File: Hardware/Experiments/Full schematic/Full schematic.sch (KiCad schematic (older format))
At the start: 31 parts

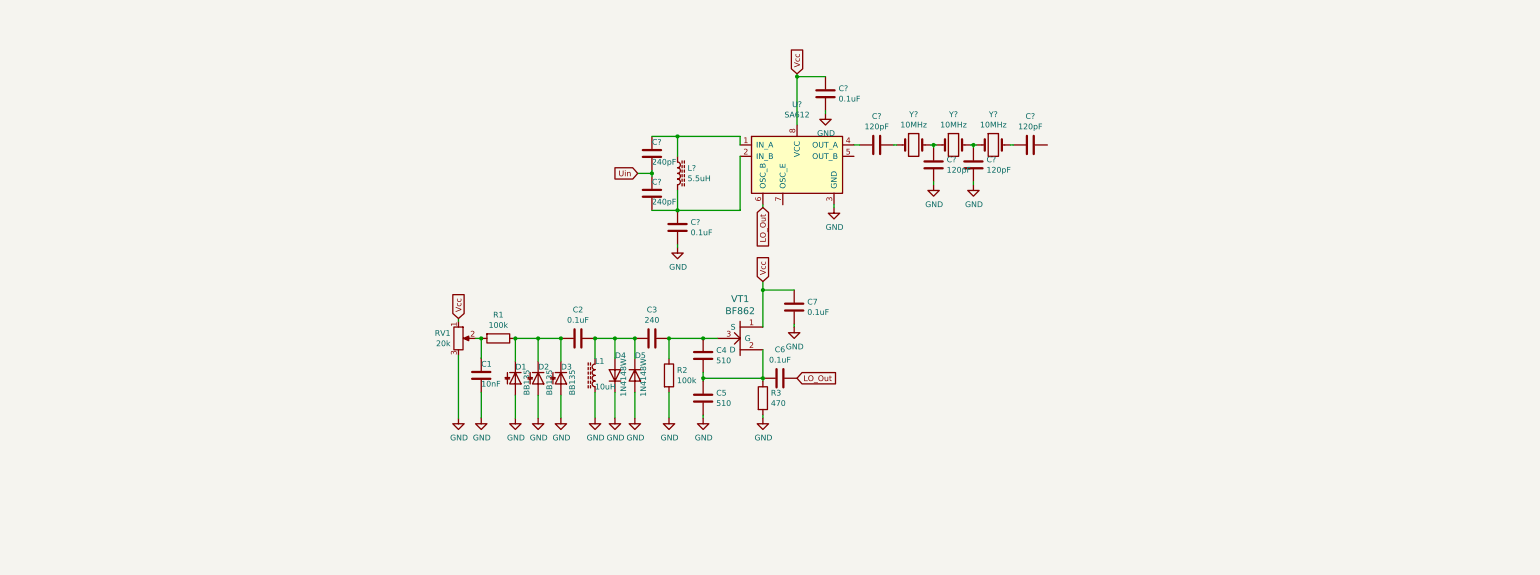
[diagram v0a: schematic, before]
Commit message: IF amplifier + second frequency convertor - tested IRL
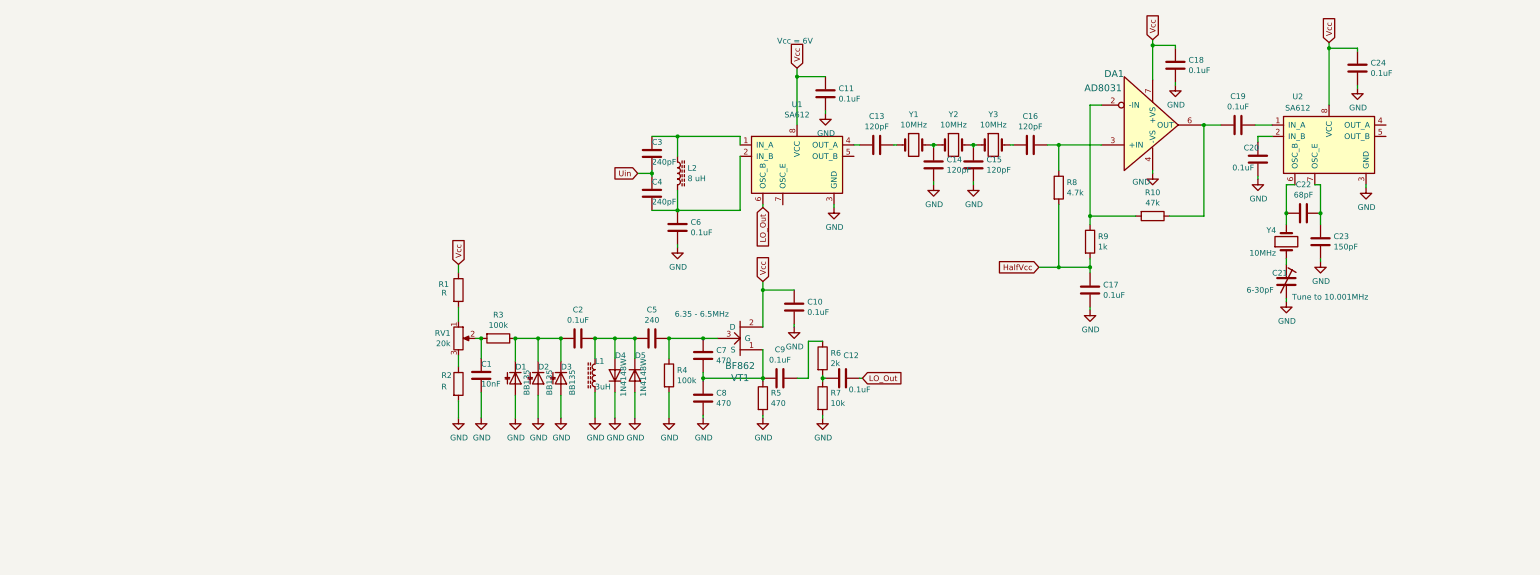
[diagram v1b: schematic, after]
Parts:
- added C12, C17, C18, C19, C20, C24: 0.1uF, symbol Device:C
- added C21: 6-30pF, symbol Device:CTRIM
- added C22: 68pF, symbol Device:C
- added C23: 150pF, symbol Device:C
- added DA1: AD8031, symbol Fossa_library:AD8031
- added R1, R2: R, symbol Device:R
- added R10: 47k, symbol Device:R
- added R6: 2k, symbol Device:R
- added R7: 10k, symbol Device:R
- added R8: 4.7k, symbol Device:R
- added R9: 1k, symbol Device:R
- added U2: SA612, symbol Fossa_library:SA612
- added Y4: 10MHz, symbol Device:Crystal
- C7: renamed from C4; value 510 -> 470
- C8: renamed from C5; value 510 -> 470
- L1: value 10uH -> 3uH
- L2: renamed from L?; value 5.5uH -> 8 uH
- gave numbers to parts that had none: 12
- renumbered C7 to C10, C3 to C5, C6 to C9, R1 to R3, R2 to R4, R3 to R5
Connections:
- net GND: now also C17.2, C18.2, C20.2, C21.2, C23.2, C24.2, DA1.4 (-VS), R2.2, R7.2, U2.3 (GND); no longer RV1.3
- net LO_Out: now also C12.1; no longer C9.1
- net Vcc: now also VT1.2 (D), C18.1, C24.1, DA1.7 (+VS), R1.1, U2.8 (VCC); no longer RV1.1, VT1.1 (S)
- net at C7.2, C8.1, C9.2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: now also VT1.1 (S); no longer VT1.2 (D)
- net at C16.2: now also DA1.3 (+IN), R8.1
- new net: R1.2, RV1.1
- new net: R2.1, RV1.3
- new net: C12.2, R6.2, R7.1
- new net: C9.1, R6.1
- new net: DA1.2 (-IN), R10.2, R9.1
- new net: C19.2, DA1.6 (OUT), R10.1
- new net: C19.1, U2.1 (IN_A)
- new net: C20.1, U2.2 (IN_B)
- new net: C22.2, U2.6 (OSC_B), Y4.2
- new net: C22.1, C23.1, U2.7 (OSC_E)
- new net: C21.1, Y4.1
- new net HalfVcc: C17.1, R8.2, R9.2
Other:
- note added: "6.35 - 6.5MHz"
- note added: "Tune to 10.001MHz"
- note added: "Vcc = 6V"

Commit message: Antenna and input amplifier
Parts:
- removed D1, D2: BB135, symbol Device:D_Capacitance
- removed R1, R2: R, symbol Device:R
- added C2: 47pF, symbol Device:C
- added C? (x3): 0.1uF, symbol Device:C
- added C?: 100pF, symbol Device:C
- added C?: 6-30pF, symbol Device:CTRIM
- added DA?: AD8031, symbol Fossa_library:AD8031
- added L?: 13uH, symbol Device:L_Core_Ferrite
- added R?: 47k, symbol Device:R
- added R?: 1k, symbol Device:R
- added R?: 4.7k, symbol Device:R
- RV1: value 20k -> 10k
- renumbered C9 to C10, C10 to C11, C11 to C12, C12 to C13, C13 to C14, C14 to C15, C15 to C16, C16 to C17, C17 to C18, C18 to C19, C19 to C20, C20 to C21, C21 to C22, C22 to C23, C23 to C24, C24 to C25, C2 to C3, C3 to C4, C4 to C5, C5 to C6, C6 to C7, C7 to C8, C8 to C9, D3 to D1, D4 to D2, D5 to D3, R3 to R1, R4 to R2, R5 to R3, R6 to R4, R7 to R5, R8 to R6, R9 to R7, R10 to R8
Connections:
- net GND: now also RV1.3, C2.2, C?.2, C?.2, C?.2, C?.2, DA?.4 (-VS), L?.1
- net HalfVcc: now also C?.1, R?.2, R?.2
- net Vcc: now also RV1.1, C?.1, DA?.7 (+VS)
- net at C3.2, D1.1 (K), R1.1: now also C2.1
- net Uin: no longer names the net of C4.2, C5.1
- net Uin: now also DA?.6 (OUT), R?.1
- new net: DA?.2 (-IN), R?.1, R?.2
- new net: C?.1, DA?.3 (+IN), R?.1
- new net: C?.1, C?.1, C?.2, L?.2
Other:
- note added: "6.5MHz -> 3.5MHz: 3.84V\n6.35MHz -> 3.65MHz: 340mV"
- note added: "9 turns on\nM400HH rod\n10mm diameter"
- note removed: "6.35 - 6.5MHz"
- moved on the sheet: C1, C10, C11, C13, C3, C6, C8, C9, D1, D2, D3, L1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

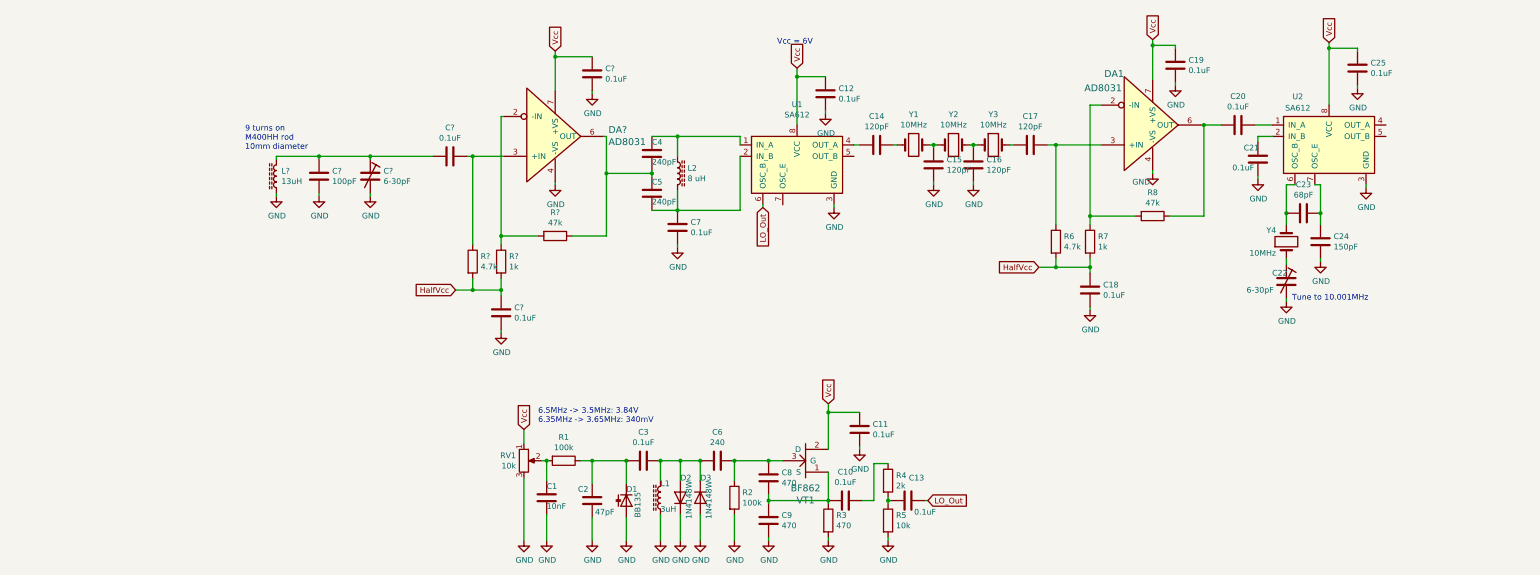
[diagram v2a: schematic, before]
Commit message: Started schematic design
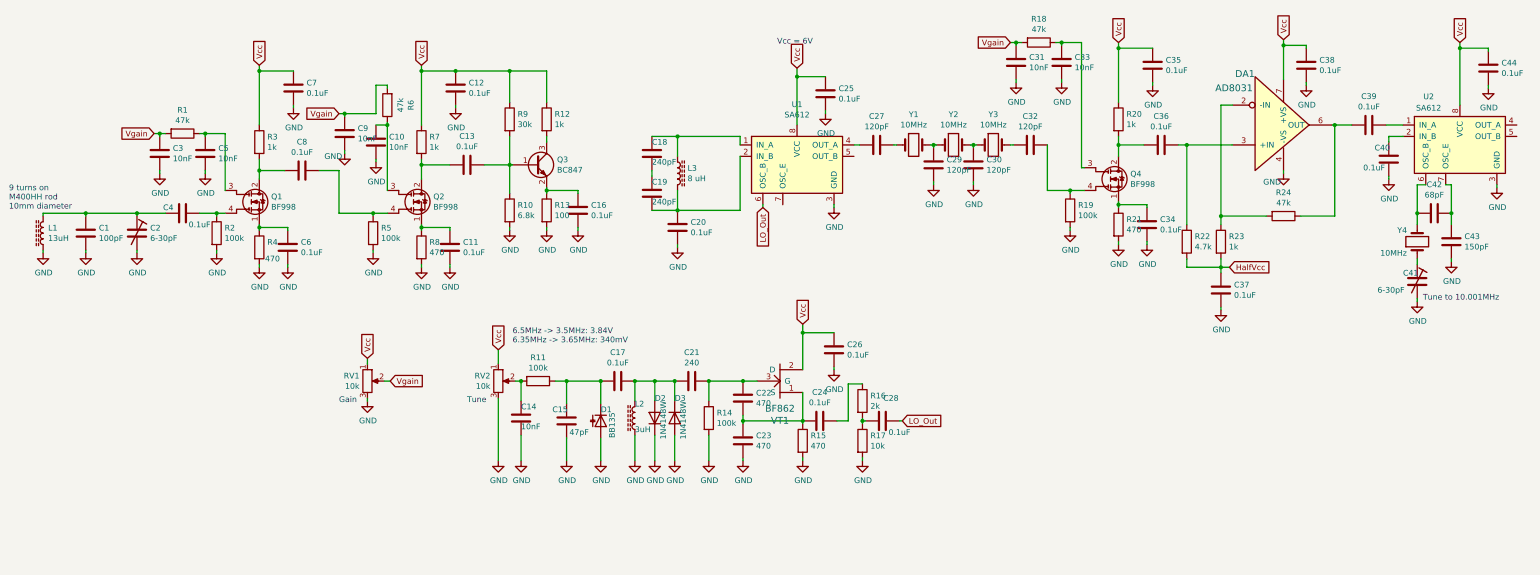
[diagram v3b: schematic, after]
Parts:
- removed C? (x3): 0.1uF, symbol Device:C
- removed DA?: AD8031, symbol Fossa_library:AD8031
- removed R?: 47k, symbol Device:R
- removed R?: 1k, symbol Device:R
- removed R?: 4.7k, symbol Device:R
- added C10, C3, C31, C33, C5, C9: 10nF, symbol Device:C
- added C11, C12, C13, C16, C34, C35, C36, C4, C6, C7, C8: 0.1uF, symbol Device:C
- added Q1, Q2, Q4: BF998, Package_TO_SOT_SMD:SOT-143, symbol Fossa_library:BF998
- added Q3: BC847, Package_TO_SOT_SMD:SOT-23, symbol Transistor_BJT:BC847
- added R1, R18, R6: 47k, symbol Device:R
- added R10: 6.8k, symbol Device:R
- added R12, R20, R3, R7: 1k, symbol Device:R
- added R13: 100, symbol Device:R
- added R19, R2, R5: 100k, symbol Device:R
- added R21, R4, R8: 470, symbol Device:R
- added R9: 30k, symbol Device:R
- added RV1: 10k, symbol Device:R_POT
- gave numbers to parts that had none: 3
- renumbered C1 to C14, C2 to C15, C3 to C17, C4 to C18, C5 to C19, C7 to C20, C6 to C21, C8 to C22, C9 to C23, C10 to C24, C12 to C25, C11 to C26, C14 to C27, C13 to C28, C15 to C29, C16 to C30, C17 to C32, C18 to C37, C19 to C38, C20 to C39, C21 to C40, C22 to C41, C23 to C42, C24 to C43, C25 to C44, L1 to L2, L2 to L3, R1 to R11, R2 to R14, R3 to R15, R4 to R16, R5 to R17, R6 to R22, R7 to R23, R8 to R24, RV1 to RV2
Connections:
- net GND: now also C10.2, C11.2, C12.2, C16.2, C3.2, C31.2, C33.2, C34.2, C35.2, C5.2, C6.2, C7.2, C9.2, R10.2, R13.2, R19.2, R2.2, R21.2, R4.2, R5.2, R8.2, RV1.3
- net Vcc: now also C12.1, C35.1, C7.1, R12.1, R20.1, R3.1, R7.1, R9.1, RV1.1
- net at DA1.3 (+IN), R22.1: now also C36.1; no longer C32.2
- net at C1.1, C2.1, L1.2: now also C4.2
- new net: C32.2, Q4.4 (G1), R19.1
- new net: C6.1, Q1.1 (S), R4.1
- new net: C8.2, Q1.2 (D), R3.2
- new net: C5.1, Q1.3 (G2), R1.1
- new net: C4.1, Q1.4 (G1), R2.1
- new net: C8.1, Q2.4 (G1), R5.1
- new net: C11.1, Q2.1 (S), R8.1
- new net: C13.2, Q2.2 (D), R7.2
- new net: C10.1, Q2.3 (G2), R6.1
- new net: C36.2, Q4.2 (D), R20.2
- new net: C34.1, Q4.1 (S), R21.1
- new net: C33.1, Q4.3 (G2), R18.1
- new net: C13.1, Q3.1 (B), R10.1, R9.2
- new net: C16.1, Q3.2 (E), R13.1
- new net: Q3.3 (C), R12.2
- new net Vgain: C3.1, C31.1, C9.1, R1.2, R18.2, R6.2, RV1.2
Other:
- note added: "Gain"
- note added: "Tune"
- moved on the sheet: C1, C14, C15, C17, C2, C21, C22, C23, C24, C26, C28, C37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
